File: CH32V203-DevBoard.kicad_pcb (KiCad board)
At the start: 2 copper layers, 20.3 x 50.8 mm, 44 parts, among them J1 USB_C_Receptacle_USB2.0_16P, J2 USB_C_Receptacle_USB2.0_16P, Q1 AO3401A, Q2 AO3401A, SW1 SW_Push, SW2 SW_Push, U1 CH32V203C8T6, U2 RT9080-33GJ5

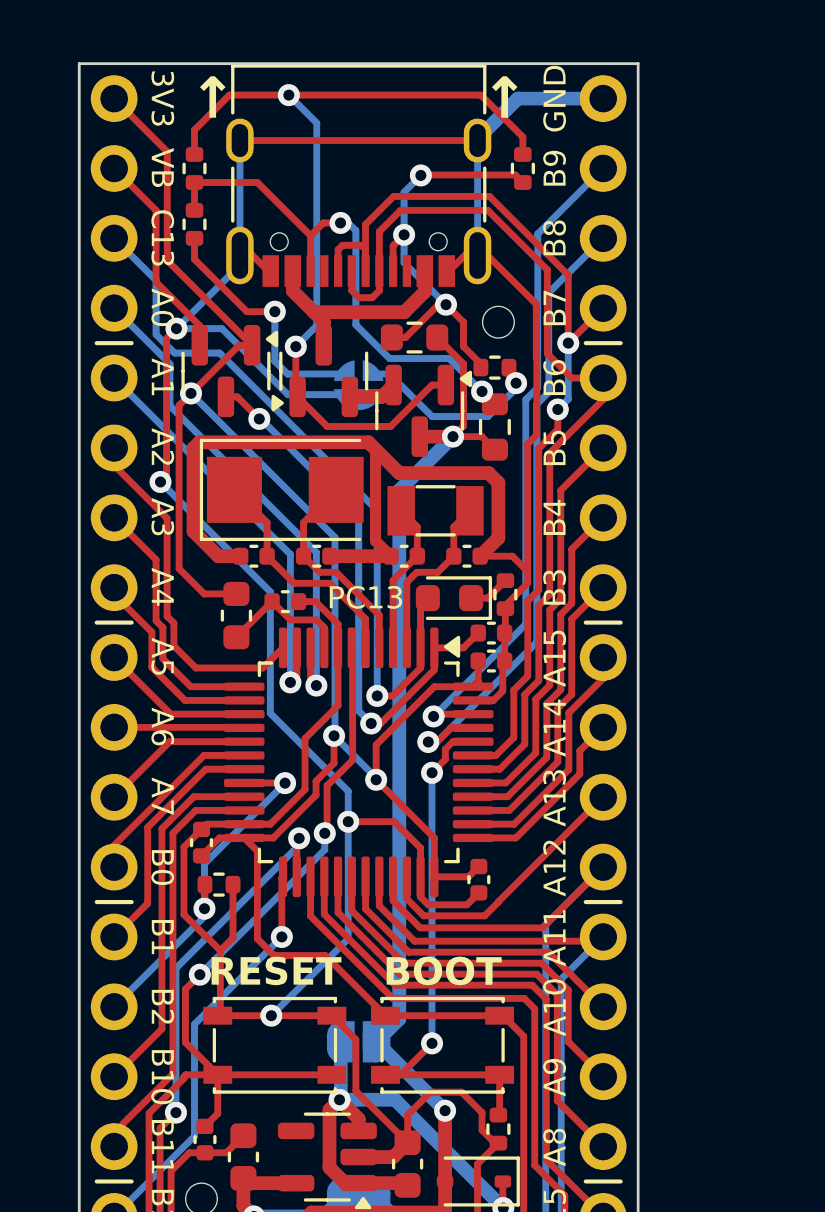
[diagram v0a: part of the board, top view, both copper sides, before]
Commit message: jumper footprint fix
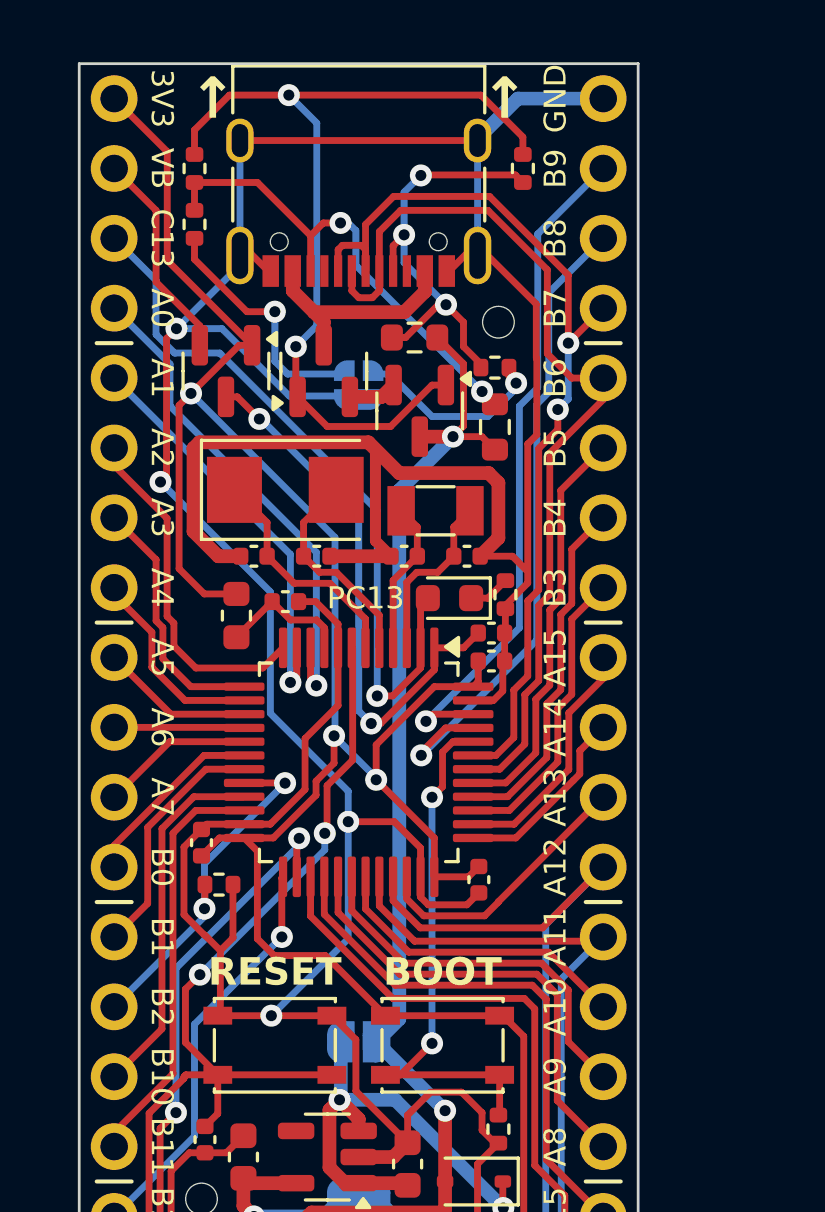
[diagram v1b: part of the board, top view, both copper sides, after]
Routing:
- net Net-(J2-CC2): track 19.0 -> 17.7 mm
- net PB8: track 23.0 -> 23.9 mm
- net PB9: track 23.9 -> 24.6 mm

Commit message: delete mosfet
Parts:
- removed Q1, Q2: AO3401A, Package_TO_SOT_SMD:SOT-23
- removed R8, R9: 1MΩ, Resistor_SMD:R_0402_1005Metric
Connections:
- J2 pad A4: Net-(Q2-D) -> VBUS
- J2 pad A9: Net-(Q2-D) -> VBUS
- J2 pad B4: Net-(Q2-D) -> VBUS
- J2 pad B9: Net-(Q2-D) -> VBUS
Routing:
- net Net-(Q1-G): track 32.9 -> 0.00 mm, vias 2 -> 0
- net VBUS: track 45.9 -> 59.9 mm
- net Net-(Q2-D): track 8.54 -> 0.00 mm
- net Net-(J2-CC1): track 16.2 -> 10.6 mm, vias 3 -> 2
- net Net-(JP3-A): track 7.25 -> 5.46 mm
- net Net-(Q1-S): track 1.77 -> 0.00 mm
- net PB7: track 34.5 -> 35.2 mm
- net Net-(J2-CC2): track 17.7 -> 17.1 mm
- net +5V: track 41.7 -> 41.1 mm
- net PB6: track 33.6 -> 34.1 mm

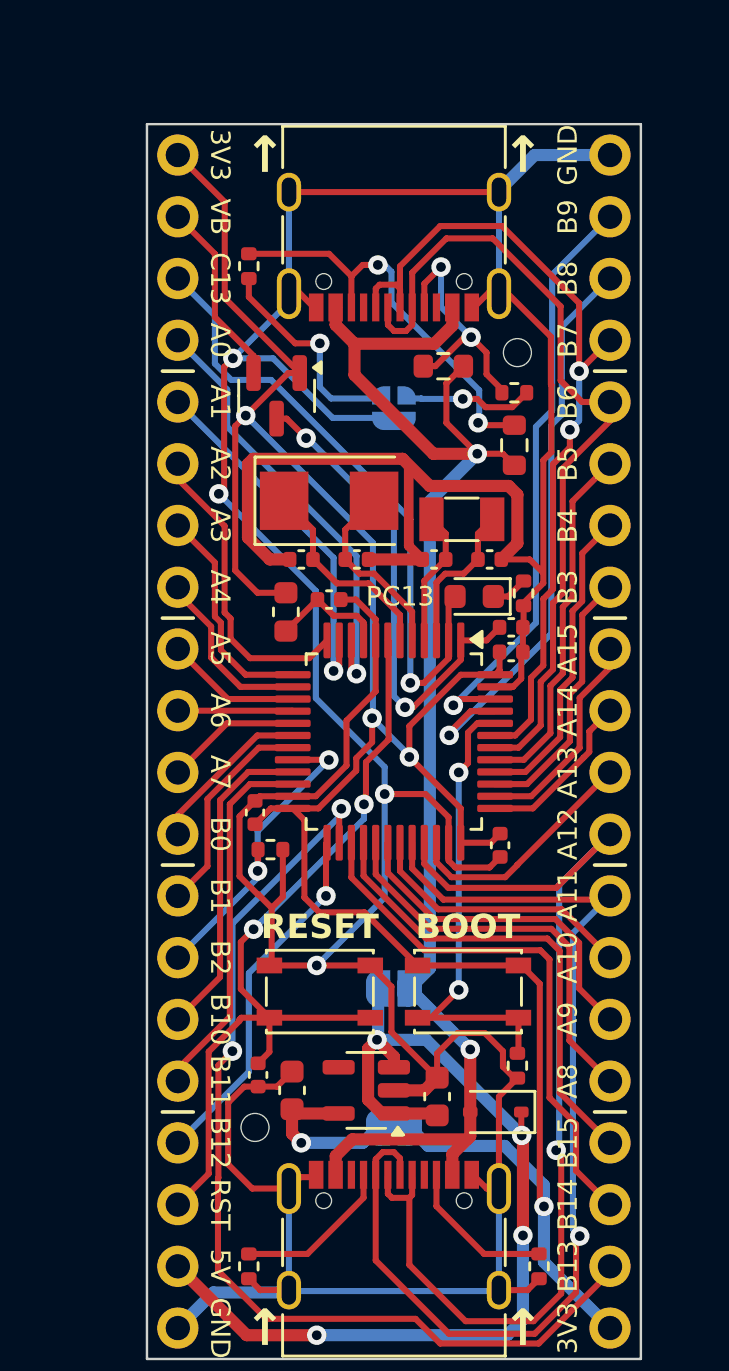
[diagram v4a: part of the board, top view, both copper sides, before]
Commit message: change ldo and add PA0 switch
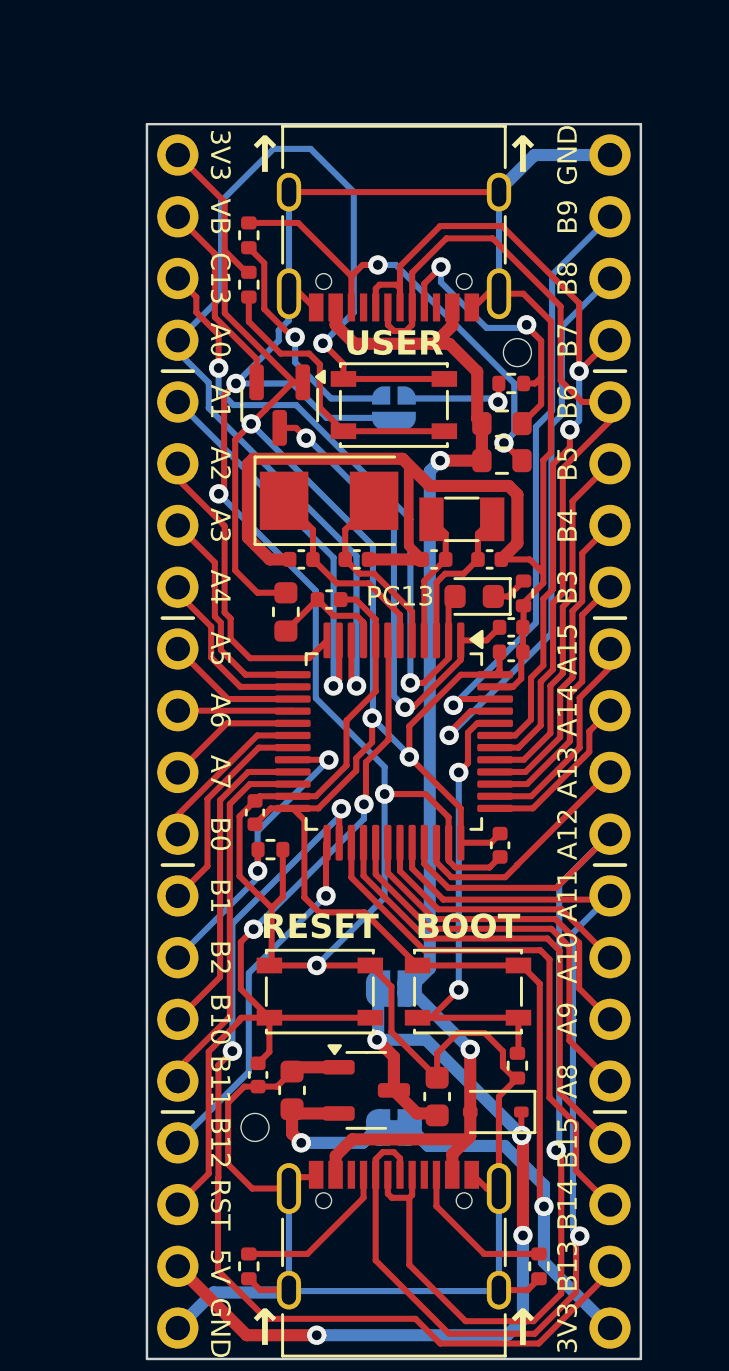
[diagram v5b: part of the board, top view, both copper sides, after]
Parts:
- added R8: 10kΩ, Resistor_SMD:R_0402_1005Metric, F.Cu at (131.2, 82.8)
- added SW3: SW_Push, Button_Switch_SMD:SW_SPST_PTS810, F.Cu at (137.2, 87.8)
- C11: value 10uF -> 1uF
- C12: value 22uF -> 1uF
- U2: value RT9080-33GJ5 -> XC6206P332MR; footprint Package_TO_SOT_SMD:TSOT-23-5 -> Package_TO_SOT_SMD:SOT-23-3
- moved R6 3.38 mm to (141.6, 88.5), turned to 180 degrees
- moved R11 1.27 mm to (131.2, 80.8)
- moved R7 0.81 mm to (141.6, 90.0), turned to 180 degrees
- moved D2 0.40 mm to (132.5, 87.8)
- moved R10 0.40 mm to (142.0, 86.9), turned to 0 degrees
- turned U2 to 0 degrees
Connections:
- U2 pad 1: +5V -> GND
- U2 pad 2: GND -> Net-(JP1-A)
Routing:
- net PA0: track 18.2 -> 45.5 mm, vias 1 -> 2
- net Net-(R8-Pad2): track 0.00 -> 12.0 mm
- net VBUS: track 59.9 -> 52.9 mm
- net +5V: track 41.1 -> 38.5 mm
- net Net-(J2-CC2): track 17.1 -> 19.0 mm
- net Net-(J2-CC1): track 10.6 -> 12.4 mm
- net PA1: track 15.1 -> 16.3 mm
- net +3V3: track 97.9 -> 99.1 mm
- net Net-(JP3-A): track 5.46 -> 4.72 mm
- net Net-(JP3-B): track 9.11 -> 9.85 mm
- net PC13: track 26.2 -> 26.8 mm, vias 1 -> 2

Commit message: USBFS resistor fix
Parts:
- R10, R11: value 4.7kΩ -> 5.1kΩ
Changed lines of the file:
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@@
 			)
 		)
-		(property "Value" "4.7kΩ"
+		(property "Value" "5.1kΩ"
 			(at 0 1.17 0)
 			(layer "F.Fab")
@@
 			)
 		)
-		(property "LCSC" "C25900"
+		(property "LCSC" "C25905"
 			(at 0 0 0)
 			(unlocked yes)
@@
 			)
 		)
-		(property "Value" "4.7kΩ"
+		(property "Value" "5.1kΩ"
 			(at 0 1.17 -90)
 			(layer "F.Fab")
@@
 			)
 		)
-		(property "LCSC" "C25900"
+		(property "LCSC" "C25905"
 			(at 0 0 90)
 			(unlocked yes)
